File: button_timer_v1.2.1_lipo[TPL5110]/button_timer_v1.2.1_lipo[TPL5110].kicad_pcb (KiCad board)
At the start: 2 copper layers, 21 x 41.7 mm, 23 parts, among them J1 Conn_01x05_Female, SW1 SW_Push, SW2 SW_Push, U2 AP2112K-3.3, U3 TPL5111, X1 ESP-12E

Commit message: 23.02 13:31
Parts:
- removed U3: TPL5111, handsolder:SOT-23-6handsoldering
- added Q1: TSM2301ACX, Package_TO_SOT_SMD:SOT-23, B.Cu at (133.2, 73.7)
- added U1: TPL5110, handsolder:SOT-23-6handsoldering, B.Cu at (134.6, 69.6)
- C4: moved to B.Cu
- C5: footprint Capacitor_SMD:C_0805_2012Metric_Pad1.18x1.45mm_HandSolder -> handsolder:C_0805_2012handsodermod
- R7: value 10k -> 100k; moved to B.Cu
- moved R7 18.9 mm to (129.8, 82.9)
- moved U2 18.7 mm to (125.3, 83.1), turned to 180 degrees
- moved R8 16.3 mm to (135.6, 65.3)
- moved D1 15.4 mm to (134.2, 61.6)
- moved C3 14.8 mm to (121.0, 83.1), turned to 90 degrees
- moved C4 14.3 mm to (135.9, 73.2), turned to 270 degrees
- moved R6 13.9 mm to (133.0, 61.6)
- moved C5 10.3 mm to (132.1, 69.6), turned to 90 degrees
- moved D2 2.44 mm to (124.4, 71.2)
- moved C1 1.28 mm to (131.3, 65.3)
- moved SW2 0.25 mm to (120.4, 72.9)
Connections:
- C5 pad 1: Net-(BT1-Pad1) -> /GND
- C5 pad 2: /GND -> Net-(BT1-Pad1)
- R7 pad 1: Net-(R7-Pad1) -> Net-(Q1-Pad3)
- U2 pad 1: Net-(BT1-Pad1) -> Net-(Q1-Pad3)
- U2 pad 3: Net-(R7-Pad1) -> Net-(R7-Pad2)
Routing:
- net Net-(Q1-Pad3): track 0.00 -> 15.0 mm
- net /RST: track 54.2 -> 41.3 mm, vias 5 -> 2
- net /GND: track 96.8 -> 88.6 mm, vias 5 -> 7
- net Net-(R7-Pad1): track 8.05 -> 0.00 mm, vias 1 -> 0
- net Net-(R7-Pad2): track 0.00 -> 2.95 mm, vias 1 -> 0
- net Net-(D2-Pad2): track 5.21 -> 2.68 mm
- net Net-(Q1-Pad1): track 0.00 -> 1.98 mm
- net /GPIO4: track 20.2 -> 21.9 mm, vias 2 -> 3
- net /VCC: track 42.3 -> 43.2 mm, vias 6 -> 2
- net Net-(BT1-Pad1): track 26.7 -> 25.9 mm, vias 4 -> 0
- net Net-(R6-Pad2): track 19.4 -> 20.0 mm, vias 0 -> 2
- net /EN: track 15.5 -> 15.2 mm, vias 2 -> 0
- net /TX: track 14.5 -> 14.3 mm, vias 0 -> 1
- net /RX: track 9.75 -> 9.67 mm, vias 1 -> 0
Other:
- board text added: "Button - LIPO v.1.2.1 TIMER 5110"
- board text added: "V1.2.1 ONLY LIPO TIMER TPL5110"
- board text removed: "Button - LIPO v.1.2.1"
- board text removed: "V1.2.1 ONLY LIPO TIMER TPL51111"

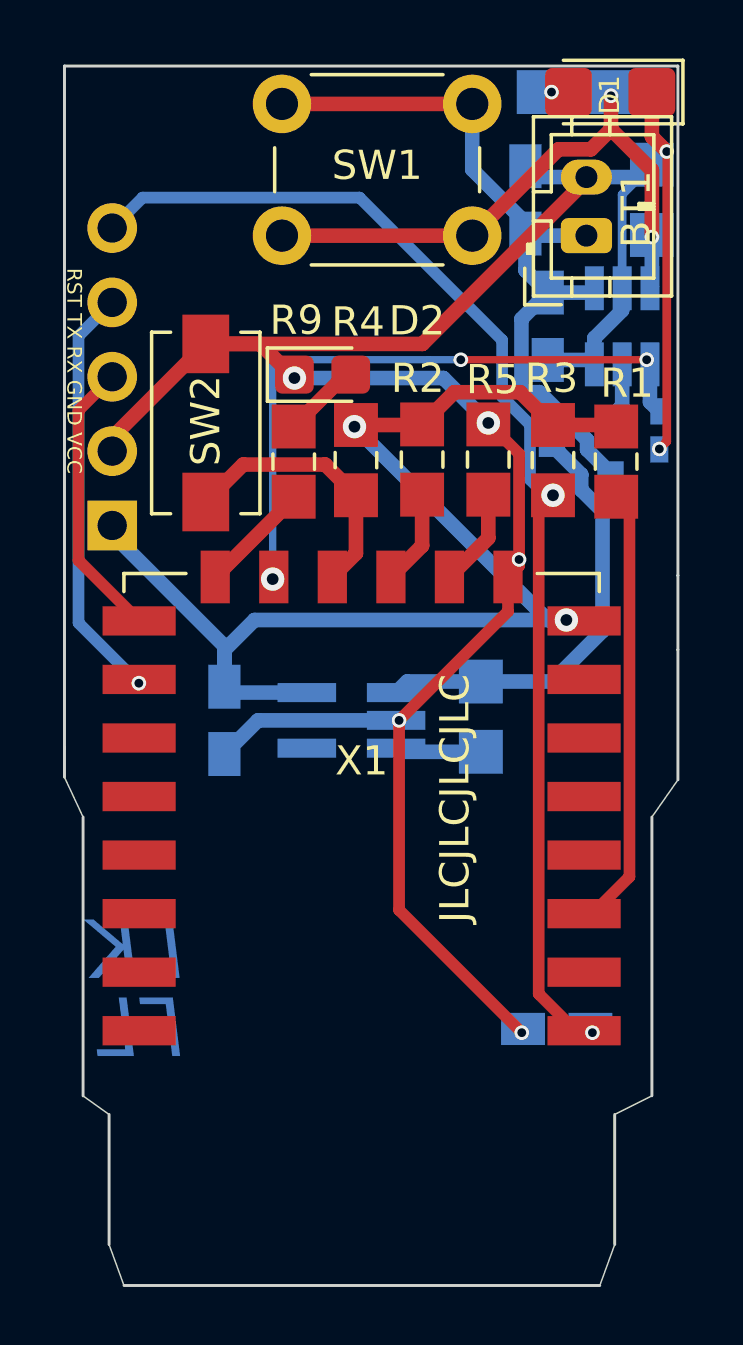
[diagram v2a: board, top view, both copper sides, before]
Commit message: 3D Models etwas verbessert
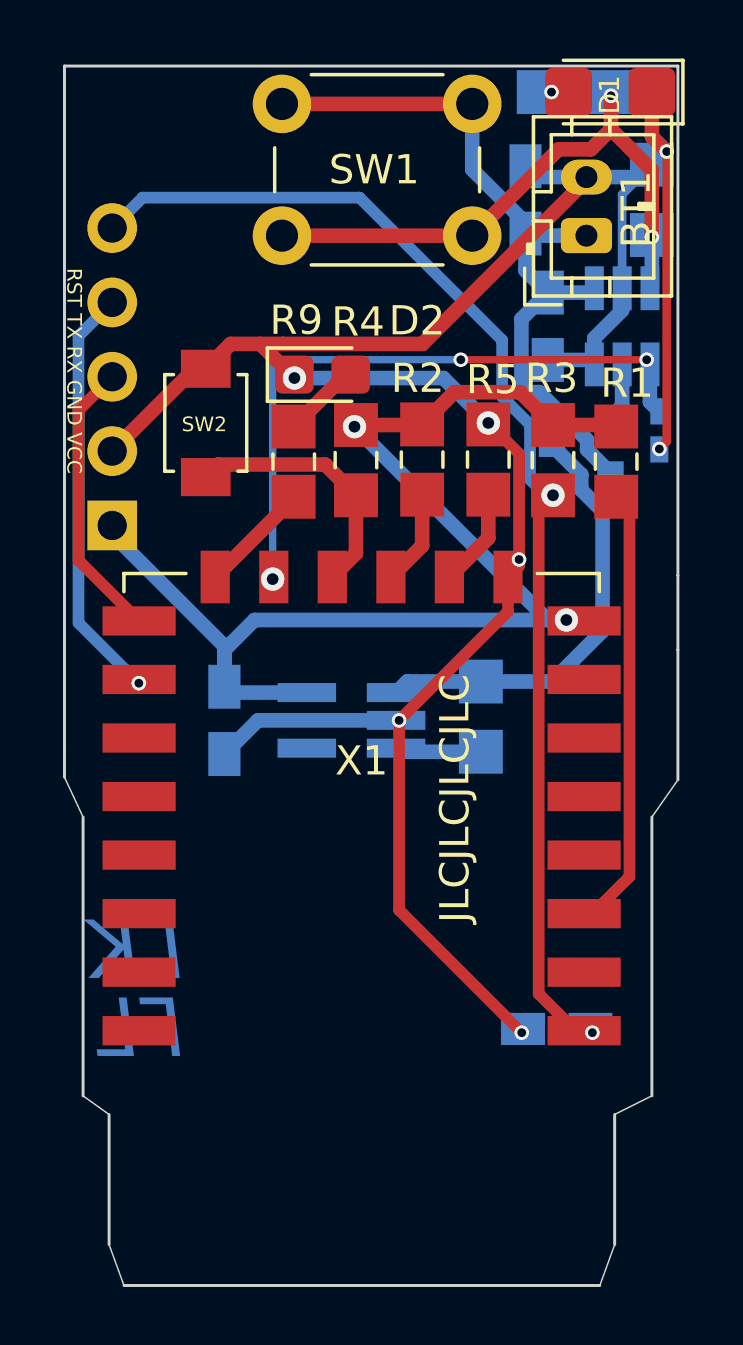
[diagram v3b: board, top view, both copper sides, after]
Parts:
- J1: footprint Connector_PinHeader_2.54mm:PinHeader_1x05_P2.54mm_Vertical -> handsolder:PinSocket_1x05_P2.54mm_Vertical_mod
- SW1: footprint Button_Switch_THT:SW_PUSH_6mm -> handsolder:SW_PUSH_6mm_H8mm_mod
- SW2: footprint Button_Switch_SMD:SW_SPST_EVQPE1 -> handsolder:SW_SPST_B3U-1000P_mod
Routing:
- net /GND: track 88.6 -> 86.5 mm

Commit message: Silkscreen Update
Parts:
- D2: footprint LED_SMD:LED_0805_2012Metric_Castellated -> handsolder:LED_0805_2012Metric_Castellated_mod
- Q1: footprint Package_TO_SOT_SMD:SOT-23 -> handsolder:SOT-23_mod

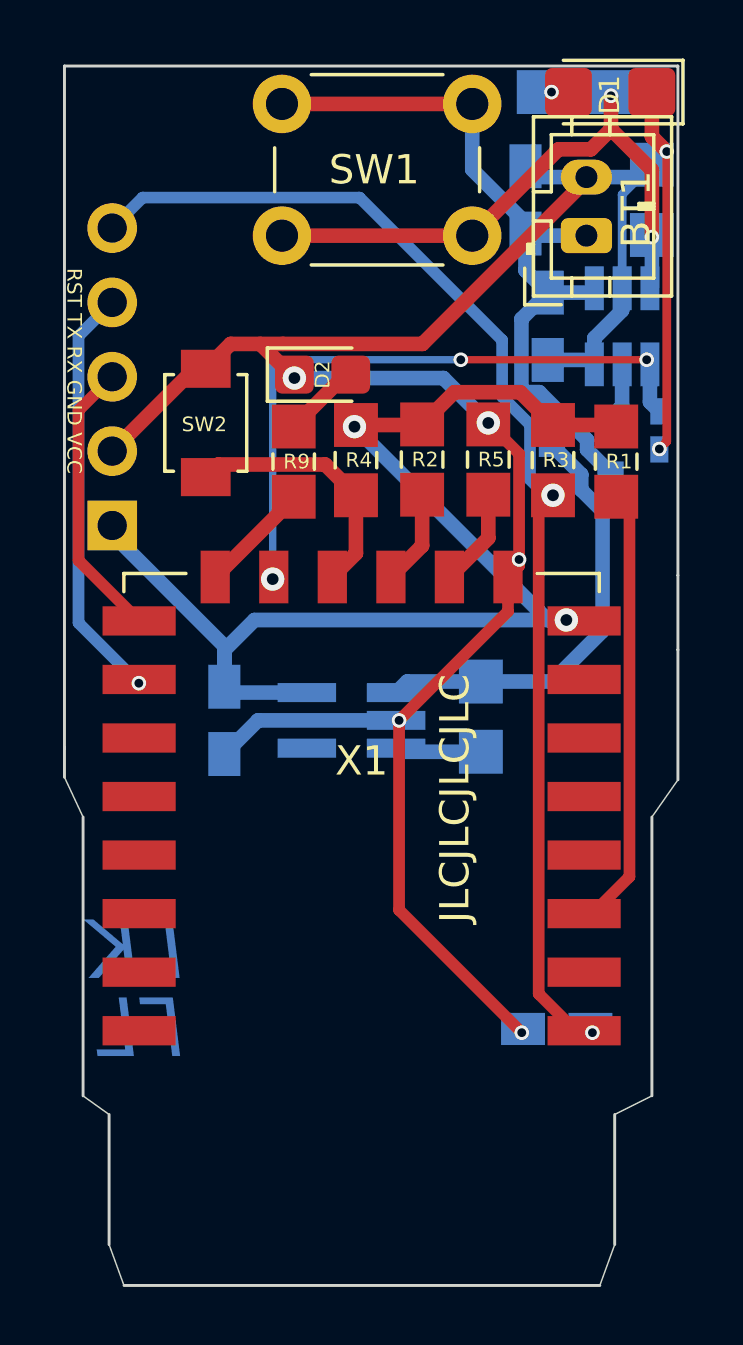
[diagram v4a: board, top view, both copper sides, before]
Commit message: cap between esp vcc and ground added
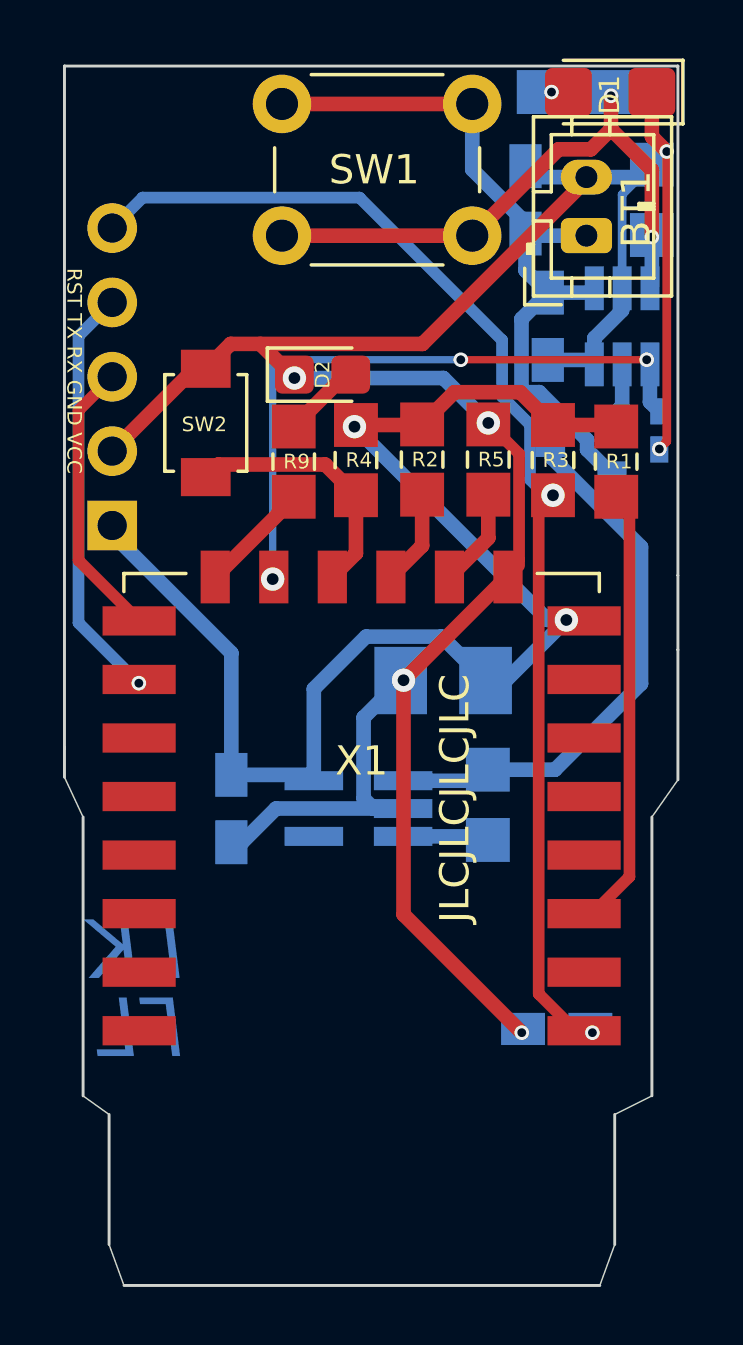
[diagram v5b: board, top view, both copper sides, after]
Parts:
- added C6: 47uF, SamacSys_Parts:CAPPM3528X210N, B.Cu at (128.5, 81.7)
- Q1: footprint handsolder:SOT-23_mod -> handsolder:SOT-23
- moved C3 3.02 mm to (121.3, 86.1)
- moved U2 3.02 mm to (125.6, 86.1)
- moved R7 3.02 mm to (130.0, 85.9)
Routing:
- net /GND: track 86.5 -> 91.9 mm, vias 7 -> 6
- net Net-(Q1-Pad3): track 15.0 -> 18.9 mm
- net /VCC: track 43.2 -> 46.9 mm
